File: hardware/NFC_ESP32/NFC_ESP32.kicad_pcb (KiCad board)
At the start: 2 copper layers, 90 x 50 mm, 62 parts, among them J1 USB_C_Receptacle_USB2.0_14P, J2 Conn_01x02, Q1 BSS138, Q2 BSS138, Q3 DMG2301L, Q5 MMBT3904, SW1 SW_SPST, U1 ESP32-WROOM-32D, U2 CH340C, U3 MCP73831-2-OT, U4 AP2112K-3.3, U5 RC522, Y1 Crystal 27.12MHz

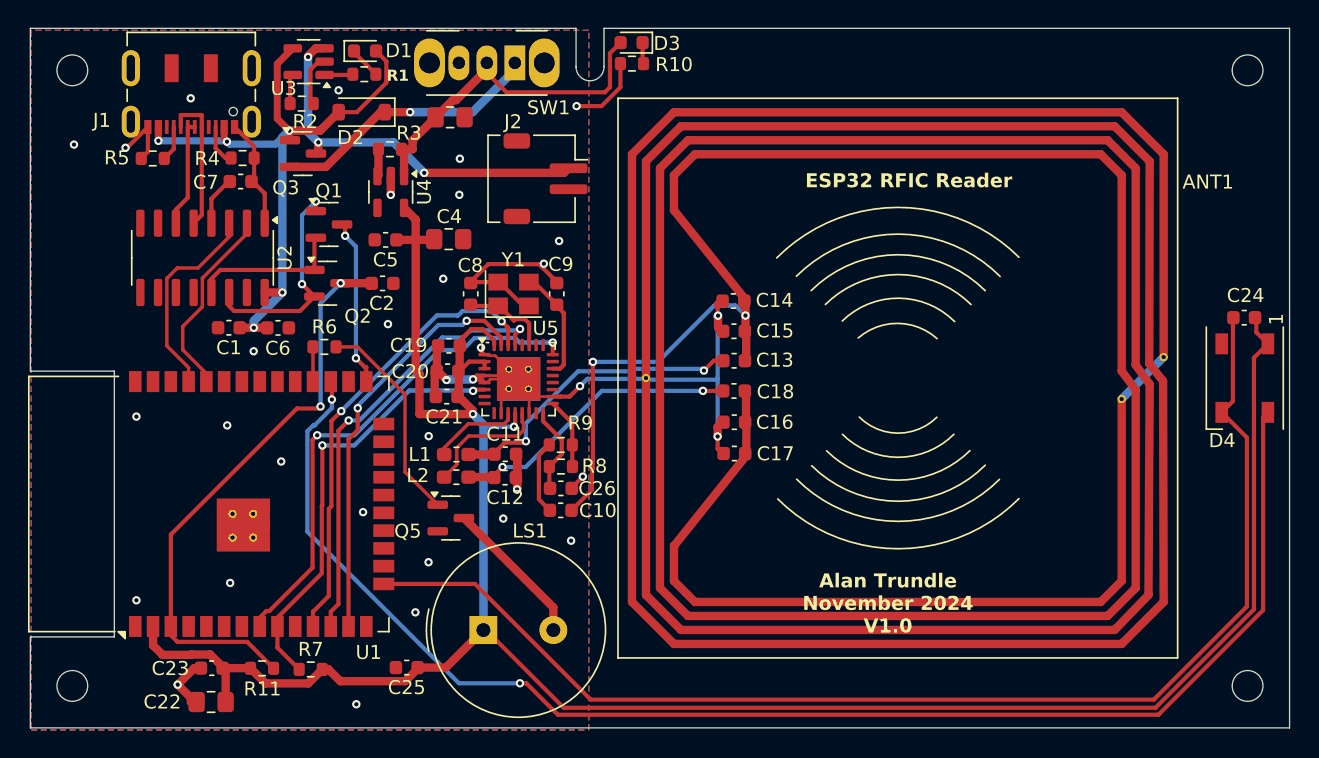
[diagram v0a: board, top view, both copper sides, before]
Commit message: Changed to resolve issues on Version 1.0
Change RC522 symbol and fix crystal pins
Swap D- and D+
Move OLED and buzzer pins
Power AVDD on RC522
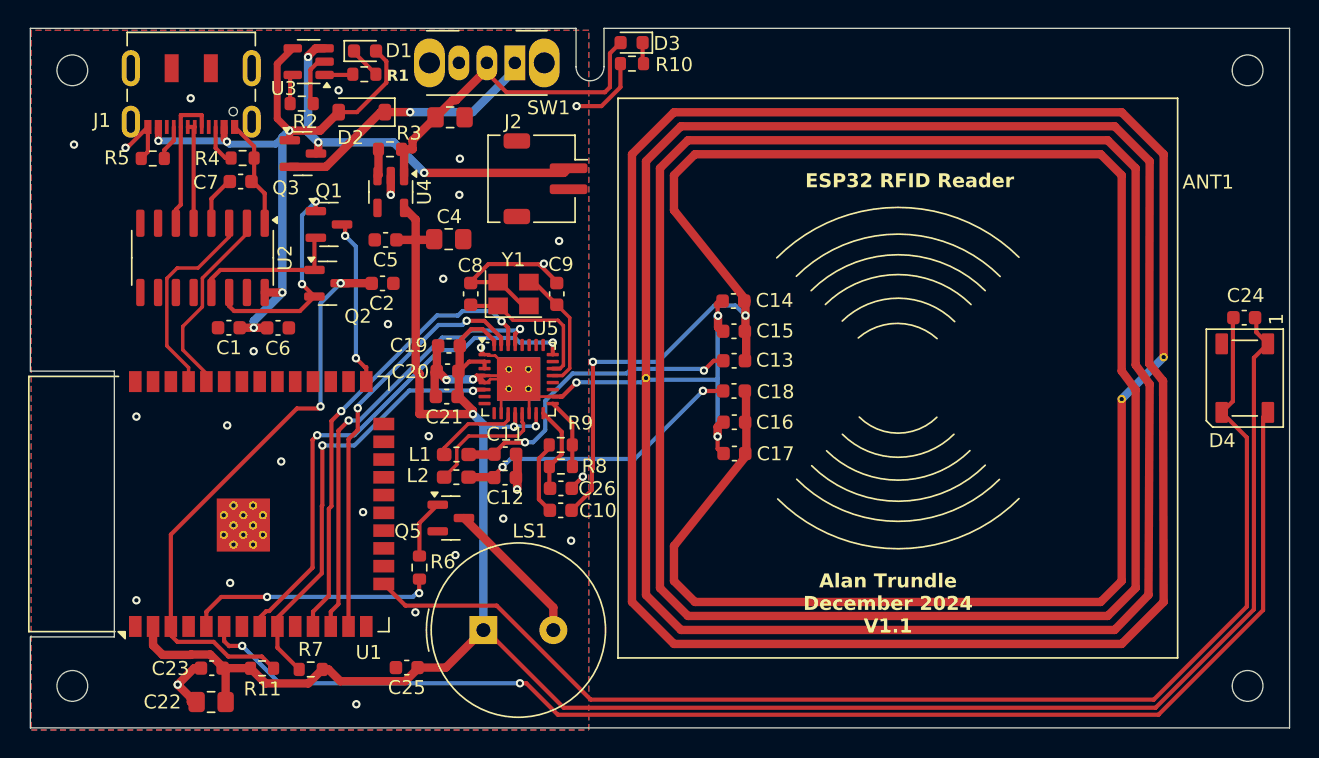
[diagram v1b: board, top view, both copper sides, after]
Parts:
- U1: footprint RFID:ESP32-WROOM-32D -> RF_Module:ESP32-WROOM-32D
- moved R6 17.2 mm to (127.8, 68.5), turned to 90 degrees
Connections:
- C8 pad 1: Net-(U5-OSCIN) -> Net-(U5-OSCOUT)
- C9 pad 1: Net-(U5-OSCOUT) -> Net-(U5-OSCIN)
- J1 pad A6: Net-(U2-UD-) -> Net-(U2-UD+)
- J1 pad A7: Net-(U2-UD+) -> Net-(U2-UD-)
- J1 pad B6: Net-(U2-UD-) -> Net-(U2-UD+)
- J1 pad B7: Net-(U2-UD+) -> Net-(U2-UD-)
- R6 pad 1: Net-(U1-IO17) -> Net-(U1-SENSOR_VN)
- U1 pad 27: Net-(D4-DIN) -> unconnected-(U1-IO16-Pad27)
- U1 pad 28: Net-(U1-IO17) -> unconnected-(U1-IO17-Pad28)
- U1 pad 5: unconnected-(U1-SENSOR_VN-Pad5) -> Net-(U1-SENSOR_VN)
- U1 pad 6: unconnected-(U1-IO34-Pad6) -> Net-(D4-DIN)
- U5 pad 15: unconnected-(U5-AVDD-Pad15) -> +3.3V
- U5 pad 21: (no net) -> Net-(U5-OSCIN)
- U5 pad 27: Net-(U5-OSCIN) -> unconnected-(U5-D3-Pad27)
- Y1 pad 1: Net-(U5-OSCIN) -> Net-(U5-OSCOUT)
- Y1 pad 3: Net-(U5-OSCOUT) -> Net-(U5-OSCIN)
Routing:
- net Net-(U1-SENSOR_VN): track 0.00 -> 17.8 mm, vias 0 -> 2
- net Net-(Q5-B): track 15.2 -> 4.21 mm
- net Net-(D4-DIN): track 102.6 -> 94.9 mm
- net Net-(U5-OSCOUT): track 7.98 -> 11.0 mm
- net Net-(U2-UD+): track 10.3 -> 7.41 mm
- net Net-(U5-OSCIN): track 6.31 -> 9.02 mm
- net +3.3V: track 166.4 -> 168.9 mm, vias 2 -> 3
- net Net-(U1-IO17): track 2.48 -> 0.00 mm
- net Net-(U2-UD-): track 7.73 -> 10.2 mm
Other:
- board text added: "Alan Trundle December 2024 V1.1"
- board text added: "ESP32 RFID Reader"
- board text removed: "Alan Trundle November 2024 V1.0"
- board text removed: "ESP32 RFIC Reader"
